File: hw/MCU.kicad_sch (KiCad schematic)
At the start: 19 parts, among them J2 Conn_01x06, J7 Conn_01x04, SW2 SKRPACE010, SW3 SKRPACE010, U2 N32L406RBL7, Y2 XL2EL89COI-111YLC-8M

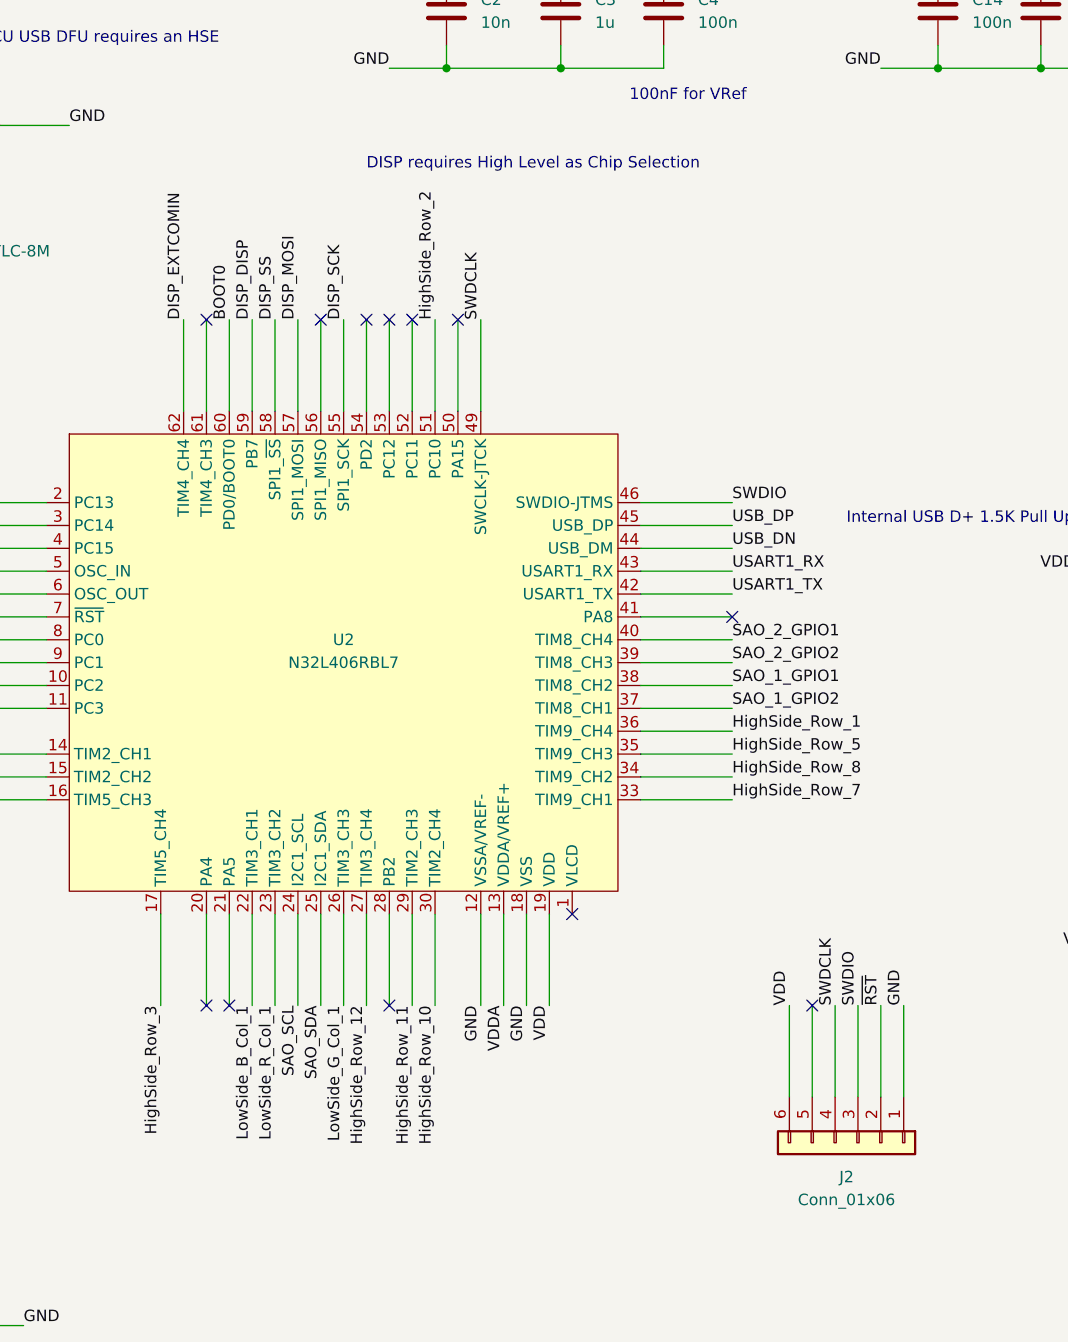
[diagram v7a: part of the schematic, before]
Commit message: re route TIM connections
mainly for connect TIM8 to LowSide RGB for using Repeat Count
connect TIM4 CH1/2/3/4 to SAO 1/2 GPIO1/2
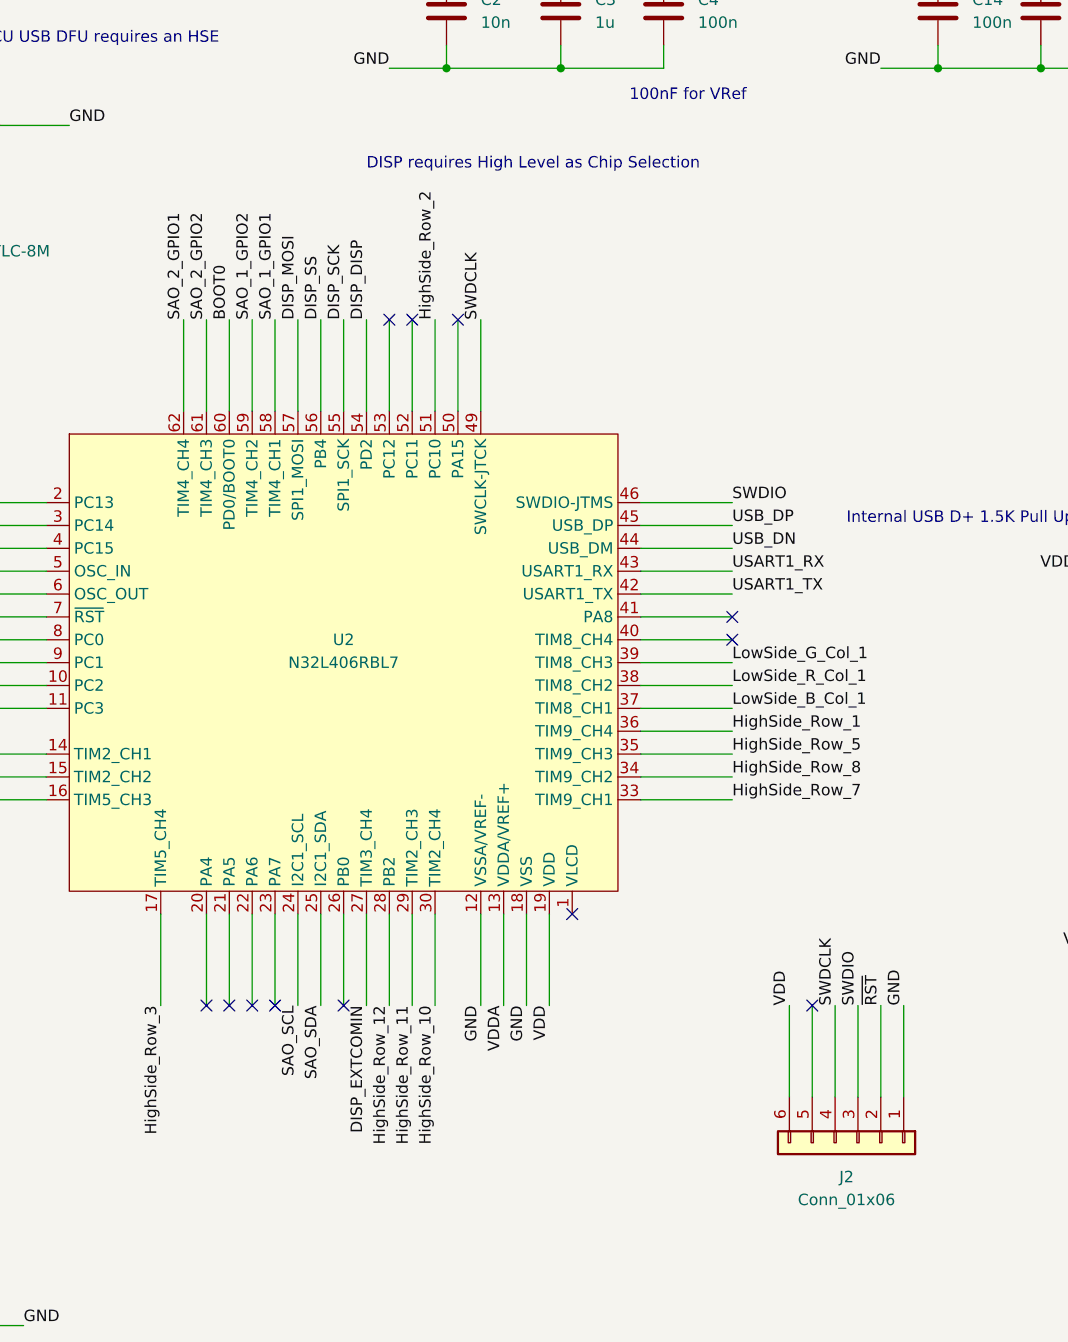
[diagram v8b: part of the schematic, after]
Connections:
- net DISP_DISP: now also U2.54 (PD2); no longer U2.59 (PB7)
- net DISP_EXTCOMIN: now also U2.27 (PB1); no longer U2.62 (PB9)
- net DISP_SS: now also U2.56 (PB4); no longer U2.58 (PB6)
- net HighSide_Row_12: now also U2.28 (PB2); no longer U2.27 (PB1)
- net LowSide_B_Col_1: now also U2.37 (PC6); no longer U2.22 (PA6)
- net LowSide_G_Col_1: now also U2.39 (PC8); no longer U2.26 (PB0)
- net LowSide_R_Col_1: now also U2.38 (PC7); no longer U2.23 (PA7)
- net SAO_1_GPIO1: now also U2.58 (PB6); no longer U2.38 (PC7)
- net SAO_1_GPIO2: now also U2.59 (PB7); no longer U2.37 (PC6)
- net SAO_2_GPIO1: now also U2.62 (PB9); no longer U2.40 (PC9)
- net SAO_2_GPIO2: now also U2.61 (PB8); no longer U2.39 (PC8)
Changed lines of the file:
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@@
   (junction (at 254 104.14) (diameter 0) (color 0 0 0 0)
   )
-  (no_connect (at 162.56 137.16))
   (no_connect (at 114.3 101.6))
   (no_connect (at 182.88 127))
   (no_connect (at 162.56 60.96))
-  (no_connect (at 142.24 60.96))
-  (no_connect (at 170.18 60.96))
+  (no_connect (at 200.66 96.52))
+  (no_connect (at 157.48 137.16))
   (no_connect (at 142.24 137.16))
+  (no_connect (at 170.18 60.96))
   (no_connect (at 200.66 93.98))
   (no_connect (at 114.3 86.36))
-  (no_connect (at 154.94 60.96))
+  (no_connect (at 149.86 137.16))
+  (no_connect (at 144.78 137.16))
   (no_connect (at 114.3 99.06))
   (no_connect (at 209.55 137.16))
   (no_connect (at 114.3 96.52))
   (no_connect (at 165.1 60.96))
-  (no_connect (at 160.02 60.96))
   (no_connect (at 114.3 81.28))
-  (no_connect (at 144.78 137.16))
   (no_connect (at 114.3 104.14))
+  (no_connect (at 147.32 137.16))
   (no_connect (at 114.3 83.82))
   (wire (pts (xy 177.8 127) (xy 177.8 137.16))
@@
     (effects (font (size 1.27 1.27)) (justify left bottom))
   )
-  (label "HighSide_Row_12" (at 160.02 137.16 270) (fields_autoplaced)
+  (label "HighSide_Row_12" (at 162.56 137.16 270) (fields_autoplaced)
     (effects (font (size 1.27 1.27)) (justify right bottom))
   )
@@
     (effects (font (size 1.27 1.27)) (justify right bottom))
   )
-  (label "DISP_EXTCOMIN" (at 139.7 60.96 90) (fields_autoplaced)
-    (effects (font (size 1.27 1.27)) (justify left bottom))
+  (label "DISP_EXTCOMIN" (at 160.02 137.16 270) (fields_autoplaced)
+    (effects (font (size 1.27 1.27)) (justify right bottom))
   )
   (label "HighSide_Row_10" (at 53.34 53.34 0) (fields_autoplaced)
@@
     (effects (font (size 1.27 1.27)) (justify right bottom))
   )
-  (label "SAO_2_GPIO2" (at 200.66 99.06 0) (fields_autoplaced)
+  (label "SAO_2_GPIO2" (at 142.24 60.96 90) (fields_autoplaced)
     (effects (font (size 1.27 1.27)) (justify left bottom))
   )
@@
     (effects (font (size 1.27 1.27)) (justify right bottom))
   )
-  (label "SAO_2_GPIO1" (at 200.66 96.52 0) (fields_autoplaced)
+  (label "SAO_2_GPIO1" (at 139.7 60.96 90) (fields_autoplaced)
     (effects (font (size 1.27 1.27)) (justify left bottom))
   )
@@
     (effects (font (size 1.27 1.27)) (justify left bottom))
   )
-  (label "LowSide_B_Col_1" (at 147.32 137.16 270) (fields_autoplaced)
-    (effects (font (size 1.27 1.27)) (justify right bottom))
+  (label "LowSide_B_Col_1" (at 200.66 104.14 0) (fields_autoplaced)
+    (effects (font (size 1.27 1.27)) (justify left bottom))
   )
   (label "DISP_EXTCOMIN" (at 53.34 129.54 0) (fields_autoplaced)
@@
     (effects (font (size 1.27 1.27)) (justify left bottom))
   )
-  (label "LowSide_G_Col_1" (at 157.48 137.16 270) (fields_autoplaced)
-    (effects (font (size 1.27 1.27)) (justify right bottom))
+  (label "LowSide_G_Col_1" (at 200.66 99.06 0) (fields_autoplaced)
+    (effects (font (size 1.27 1.27)) (justify left bottom))
   )
   (label "LowSide_R_Col_1" (at 53.34 64.77 0) (fields_autoplaced)
@@
     (effects (font (size 1.27 1.27)) (justify left bottom))
   )
-  (label "DISP_SS" (at 149.86 60.96 90) (fields_autoplaced)
+  (label "DISP_SS" (at 154.94 60.96 90) (fields_autoplaced)
     (effects (font (size 1.27 1.27)) (justify left bottom))
   )
@@
     (effects (font (size 1.27 1.27)) (justify left bottom))
   )
-  (label "SAO_1_GPIO2" (at 200.66 104.14 0) (fields_autoplaced)
+  (label "SAO_1_GPIO2" (at 147.32 60.96 90) (fields_autoplaced)
     (effects (font (size 1.27 1.27)) (justify left bottom))
   )
@@
     (effects (font (size 1.27 1.27)) (justify left bottom))
   )
-  (label "LowSide_R_Col_1" (at 149.86 137.16 270) (fields_autoplaced)
-    (effects (font (size 1.27 1.27)) (justify right bottom))
+  (label "LowSide_R_Col_1" (at 200.66 101.6 0) (fields_autoplaced)
+    (effects (font (size 1.27 1.27)) (justify left bottom))
   )
   (label "GND" (at 217.17 33.02 180) (fields_autoplaced)
@@
     (effects (font (size 1.27 1.27)) (justify left bottom))
   )
-  (label "SAO_1_GPIO1" (at 200.66 101.6 0) (fields_autoplaced)
+  (label "SAO_1_GPIO1" (at 149.86 60.96 90) (fields_autoplaced)
     (effects (font (size 1.27 1.27)) (justify left bottom))
   )
@@
     (effects (font (size 1.27 1.27)) (justify left bottom))
   )
-  (label "DISP_DISP" (at 147.32 60.96 90) (fields_autoplaced)
+  (label "DISP_DISP" (at 160.02 60.96 90) (fields_autoplaced)
     (effects (font (size 1.27 1.27)) (justify left bottom))
   )
@@
     (pin "20")
     (pin "21")
-    (pin "22" (alternate "TIM3_CH1"))
-    (pin "23" (alternate "TIM3_CH2"))
+    (pin "22")
+    (pin "23")
     (pin "24" (alternate "I2C1_SCL"))
     (pin "25" (alternate "I2C1_SDA"))
-    (pin "26" (alternate "TIM3_CH3"))
+    (pin "26")
     (pin "27" (alternate "TIM3_CH4"))
     (pin "28")
@@
     (pin "54")
     (pin "55" (alternate "SPI1_SCK"))
-    (pin "56" (alternate "SPI1_MISO"))
+    (pin "56")
     (pin "57" (alternate "SPI1_MOSI"))
-    (pin "58" (alternate "SPI1_~{SS}"))
-    (pin "59")
+    (pin "58" (alternate "TIM4_CH1"))
+    (pin "59" (alternate "TIM4_CH2"))
     (pin "6" (alternate "OSC_OUT"))
     (pin "60")
